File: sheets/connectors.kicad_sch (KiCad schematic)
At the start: 11 parts

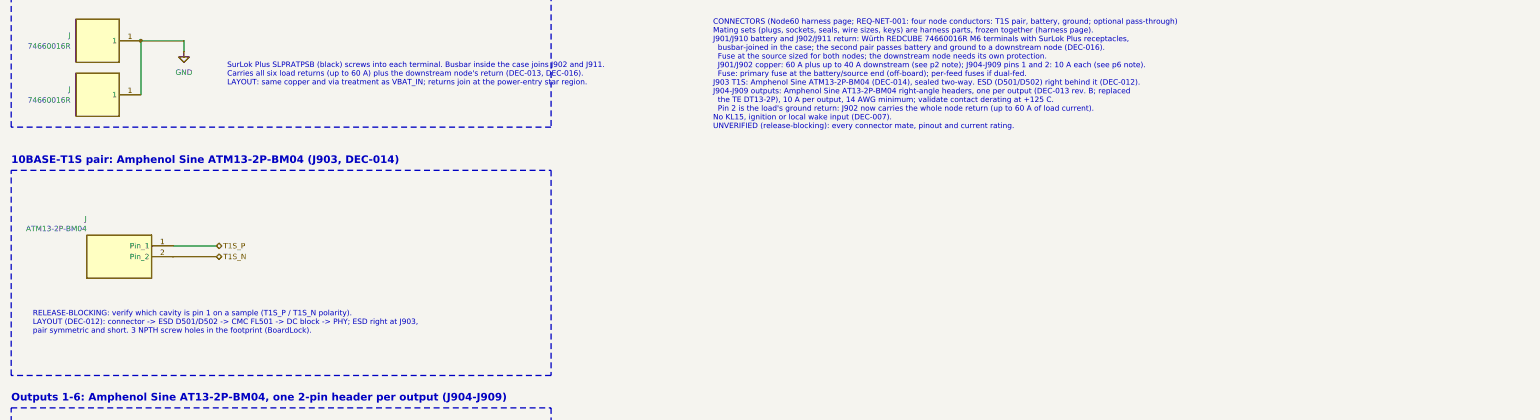
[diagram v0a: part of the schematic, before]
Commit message: DEC-017: T1S bus pass-through and relay-switched termination
The user asked for a second T1S connector so a downstream node can join
the bus, and a termination that can be switched between bus end and
mid-bus (2026-10-28).

- p9: J912, a second ATM13-2P-BM04 in parallel with J903
- p5: R502 (single 100R, not fitted) replaced by the OPEN Alliance
  split termination: latching relay K501 (Omron G6KU-2F-Y-T1-TRS DC3,
  +125 °C) selects 49.9R (end, SET) or 1.5k (drop, RESET) legs to a
  centre tap with 100nF || 100k; Q501/Q502 (DMC2710UVQ-7) half-bridges
  drive the coil from 3V3_MAIN
- p4/root: PTD0 -> T1S_TERM_END, PTD1 -> T1S_TERM_DROP
- Library pinned to dropout-kicad-library PR #37 head db07592; the new
  DropOut_Relay / DropOut_Relay_SMD libraries are in the library tables
- DEC-017, parts, GATE-NET-02 (switched termination), GATE-NET-01 wake
  test in both states, firmware and network pages, GATE-MCU-01 addendum

Co-Authored-By: Claude Opus 5.5 <noreply@anthropic.com>
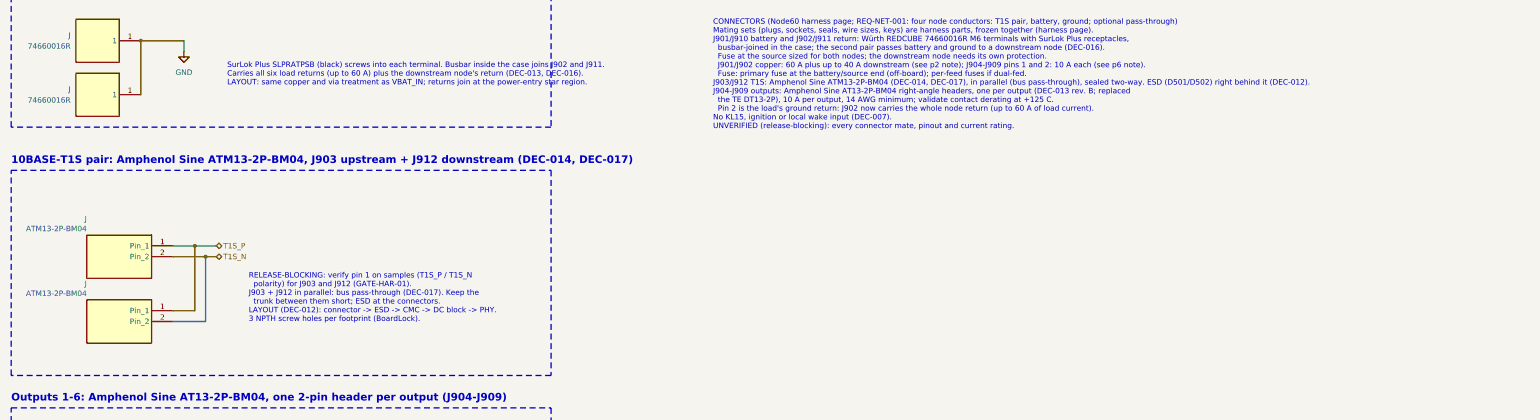
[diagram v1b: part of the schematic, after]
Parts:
- added J: ATM13-2P-BM04, DropOut_Connector_Amphenol:Amphenol_ATM13-2P-BMxx_1x02_P4.20mm_Horizontal, symbol DropOut_Connector:ATM13-2P-BM04
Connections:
- net T1S_N: now also J.2 (Pin_2)
- net T1S_P: now also J.1 (Pin_1)
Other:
- note added: "10BASE-T1S pair: Amphenol Sine ATM13-2P-BM04, J903 upstream + J912 downstream (DEC-014, DEC-017)"
- note added: "RELEASE-BLOCKING: verify pin 1 on samples (T1S_P / T1S_N polarity) for J903 and J912 (GATE-HAR-01). J903 + J912 in parallel: bus pass-through (DEC-017). Keep the trunk between them short; ESD at the connectors. LAYOUT (DEC-012): connector -> ESD -> CMC -> DC block -> PHY. 3 NPTH screw holes per footprint (BoardLock)."
- note removed: "10BASE-T1S pair: Amphenol Sine ATM13-2P-BM04 (J903, DEC-014)"
- note removed: "RELEASE-BLOCKING: verify which cavity is pin 1 on a sample (T1S_P / T1S_N polarity). LAYOUT (DEC-012): connector -> ESD D501/D502 -> CMC FL501 -> DC block -> PHY; ESD right at J903, pair symmetric and short. 3 NPTH screw holes in the footprint (BoardLock)."
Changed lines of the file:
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@@
 		)
 	)
-	(text "10BASE-T1S pair: Amphenol Sine ATM13-2P-BM04 (J903, DEC-014)"
+	(text "10BASE-T1S pair: Amphenol Sine ATM13-2P-BM04, J903 upstream + J912 downstream (DEC-014, DEC-017)"
 		(exclude_from_sim no)
 		(at 25.4 151.13 0)
@@
 		)
 	)
-	(text "RELEASE-BLOCKING: verify which cavity is pin 1 on a sample (T1S_P / T1S_N polarity).\nLAYOUT (DEC-012): connector -> ESD D501/D502 -> CMC FL501 -> DC block -> PHY; ESD right at J903,\npair symmetric and short. 3 NPTH screw holes in the footprint (BoardLock)."
-		(exclude_from_sim no)
-		(at 30.48 185.42 0)
+	(text "RELEASE-BLOCKING: verify pin 1 on samples (T1S_P / T1S_N\n  polarity) for J903 and J912 (GATE-HAR-01).\nJ903 + J912 in parallel: bus pass-through (DEC-017). Keep the\n  trunk between them short; ESD at the connectors.\nLAYOUT (DEC-012): connector -> ESD -> CMC -> DC block -> PHY.\n3 NPTH screw holes per footprint (BoardLock)."
+		(exclude_from_sim no)
+		(at 81.28 176.53 0)
 		(effects
 			(font
@@
 		)
 	)
-	(text "CONNECTORS (Node60 harness page; REQ-NET-001: four node conductors: T1S pair, battery, ground; optional pass-through)\nMating sets (plugs, sockets, seals, wire sizes, keys) are harness parts, frozen together (harness page).\nJ901/J910 battery and J902/J911 return: Würth REDCUBE 74660016R M6 terminals with SurLok Plus receptacles,\n  busbar-joined in the case; the second pair passes battery and ground to a downstream node (DEC-016).\n  Fuse at the source sized for both nodes; the downstream node needs its own protection.\n  J901/J902 copper: 60 A plus up to 40 A downstream (see p2 note); J904-J909 pins 1 and 2: 10 A each (see p6 note).\n  Fuse: primary fuse at the battery/source end (off-board); per-feed fuses if dual-fed.\nJ903 T1S: Amphenol Sine ATM13-2P-BM04 (DEC-014), sealed two-way. ESD (D501/D502) right behind it (DEC-012).\nJ904-J909 outputs: Amphenol Sine AT13-2P-BM04 right-angle headers, one per output (DEC-013 rev. B; replaced\n  the TE DT13-2P), 10 A per output, 14 AWG minimum; validate contact derating at +125 C.\n  Pin 2 is the load's ground return: J902 now carries the whole node return (up to 60 A of load current).\nNo KL15, ignition or local wake input (DEC-007).\nUNVERIFIED (release-blocking): every connector mate, pinout and current rating.\n"
+	(text "CONNECTORS (Node60 harness page; REQ-NET-001: four node conductors: T1S pair, battery, ground; optional pass-through)\nMating sets (plugs, sockets, seals, wire sizes, keys) are harness parts, frozen together (harness page).\nJ901/J910 battery and J902/J911 return: Würth REDCUBE 74660016R M6 terminals with SurLok Plus receptacles,\n  busbar-joined in the case; the second pair passes battery and ground to a downstream node (DEC-016).\n  Fuse at the source sized for both nodes; the downstream node needs its own protection.\n  J901/J902 copper: 60 A plus up to 40 A downstream (see p2 note); J904-J909 pins 1 and 2: 10 A each (see p6 note).\n  Fuse: primary fuse at the battery/source end (off-board); per-feed fuses if dual-fed.\nJ903/J912 T1S: Amphenol Sine ATM13-2P-BM04 (DEC-014, DEC-017), in parallel (bus pass-through), sealed two-way. ESD (D501/D502) right behind it (DEC-012).\nJ904-J909 outputs: Amphenol Sine AT13-2P-BM04 right-angle headers, one per output (DEC-013 rev. B; replaced\n  the TE DT13-2P), 10 A per output, 14 AWG minimum; validate contact derating at +125 C.\n  Pin 2 is the load's ground return: J902 now carries the whole node return (up to 60 A of load current).\nNo KL15, ignition or local wake input (DEC-007).\nUNVERIFIED (release-blocking): every connector mate, pinout and current rating.\n"
 		(exclude_from_sim no)
 		(at 190.5 116.84 0)
@@
 		)
 	)
+	(symbol
+		(lib_id "DropOut_Connector:ATM13-2P-BM04")
+		(at 50.8 187.96 0)
+		(mirror y)
+		(unit 1)
+		(body_style 1)
+		(exclude_from_sim no)
+		(in_bom yes)
+		(on_board yes)
+		(in_pos_files yes)
+		(dnp no)
+		(fields_autoplaced no)
+		(property "Reference" "J"
+			(at 43.18 179.07 0)
+			(effects
+				(font
+					(size 1.27 1.27)
+				)
+				(justify left)
+			)
+		)
+		(property "Value" "ATM13-2P-BM04"
+			(at 43.18 181.37 0)
+			(effects
+				(font
+					(size 1.27 1.27)
+				)
+				(justify left)
+			)
+		)
+		(property "Footprint" "DropOut_Connector_Amphenol:Amphenol_ATM13-2P-BMxx_1x02_P4.20mm_Horizontal"
+			(at 50.8 187.96 0)
+			(effects
+				(font
+					(size 1.27 1.27)
+				)
+				(hide yes)
+			)
+		)
+		(property "Datasheet" "https://www.amphenol-sine.com/pdf/datasheet/ATM13-2P-BM04.pdf"
+			(at 50.8 187.96 0)
+			(effects
+				(font
+					(size 1.27 1.27)
+				)
+				(hide yes)
+			)
+		)
+		(property "Description" "Amphenol Sine BoardLock ATM13 2-pin right-angle PCB receptacle with flange seal, 4.20 mm pitch, tin-plated size 20 pins, potting, 7.5 A, 250 V, IP67 mated, -55 to +125 °C; mates ATM06-2S"
+			(at 50.8 187.96 0)
+			(effects
+				(font
+					(size 1.27 1.27)
+				)
+				(hide yes)
+			)
+		)
+		(property "Manufacturer" "Amphenol Sine Systems"
+			(at 50.8 187.96 0)
+			(effects
+				(font
+					(size 1.27 1.27)
+				)
+				(hide yes)
+			)
+		)
+		(property "MPN" "ATM13-2P-BM04"
+			(at 50.8 187.96 0)
+			(effects
+				(font
+					(size 1.27 1.27)
+				)
+				(hide yes)
+			)
+		)
+		(property "DigiKey_PN" "889-3357-ND"
+			(at 50.8 187.96 0)
+			(effects
+				(font
+					(size 1.27 1.27)
+				)
+				(hide yes)
+			)
+		)
+		(property "Mouser_PN" "654-ATM13-2P-BM04"
+			(at 50.8 187.96 0)
+			(effects
+				(font
+					(size 1.27 1.27)
+				)
+				(hide yes)
+			)
+		)
+		(property "Temperature_Grade" "-55 to +125 °C (not AEC qualified)"
+			(at 50.8 187.96 0)
+			(effects
+				(font
+					(size 1.27 1.27)
+				)
+				(hide yes)
+			)
+		)
+		(property "Notes" "Mates the ATM06-2S plug (size 20 sockets). Fixed by 3x #4-20 thread-forming screws from the solder side (0.68-1.13 N-m). Pin numbering from the drawing's mounting-face view; verify on a sample."
+			(at 50.8 187.96 0)
+			(effects
+				(font
+					(size 1.27 1.27)
+				)
+				(hide yes)
+			)
+		)
+		(pin "1"
+		)
+		(pin "2"
+		)
+		(instances
+			(project "node60"
+				(path "/55f51841-30a3-4965-b848-b796f60054d0/e572f86f-2725-4aae-a9c5-04dc01b6640e"
+					(reference "J912")
+					(unit 1)
+				)
+			)
+		)
+	)
+	(wire
+		(pts
+			(xy 63.5 185.42)
+			(xy 68.58 185.42)
+		)
+		(stroke
+			(width 0)
+			(type default)
+		)
+	)
+	(wire
+		(pts
+			(xy 68.58 185.42)
+			(xy 68.58 170.18)
+		)
+		(stroke
+			(width 0)
+			(type default)
+		)
+	)
+	(wire
+		(pts
+			(xy 63.5 187.96)
+			(xy 71.12 187.96)
+		)
+		(stroke
+			(width 0)
+			(type default)
+		)
+	)
+	(wire
+		(pts
+			(xy 71.12 187.96)
+			(xy 71.12 172.72)
+		)
+		(stroke
+			(width 0)
+			(type default)
+		)
+	)
+	(junction
+		(at 68.58 170.18)
+		(diameter 0)
+		(color 0 0 0 0)
+	)
+	(junction
+		(at 71.12 172.72)
+		(diameter 0)
+		(color 0 0 0 0)
+	)
 	(embedded_fonts no)

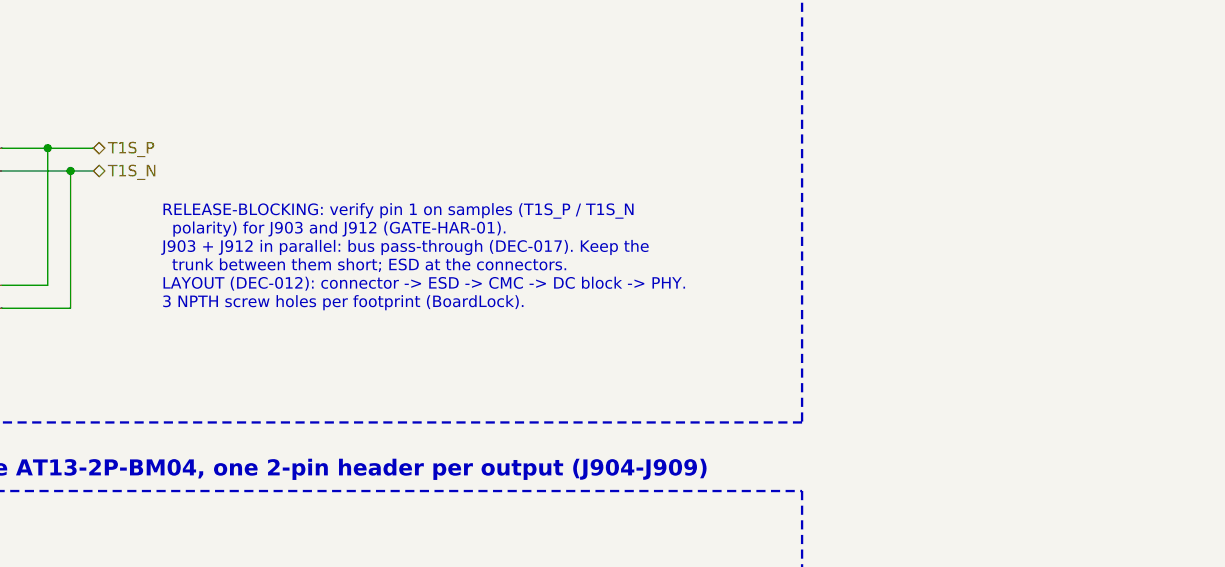
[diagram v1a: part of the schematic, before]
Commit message: DEC-012 rev. B: DC block on the connector side of the choke
Microchip AN1718 rev. D (the LAN8670 data sheet's line-interface
reference), OPEN Alliance's implementation spec (Figure 4) and both
Microchip LAN8670 evaluation boards order the line interface
connector -> ESD -> termination -> DC block -> CMC -> PHY. Node60 had
the choke on the connector side. The user approved the swap on
2026-10-29.

- p5: FL501 moved next to the PHY, C511/C512 to the bus side; no part
  changes; windings unchanged (1-4 P, 2-3 N)
- DEC-012 rev. B with the old order as a rejected option; layout notes
  on p5, p9 and in DEC-017 follow
- AN1718 and the two evaluation board schematics archived in
  dropout-vendor-docs (d4bfad3)

Co-Authored-By: Claude Opus 5.5 <noreply@anthropic.com>
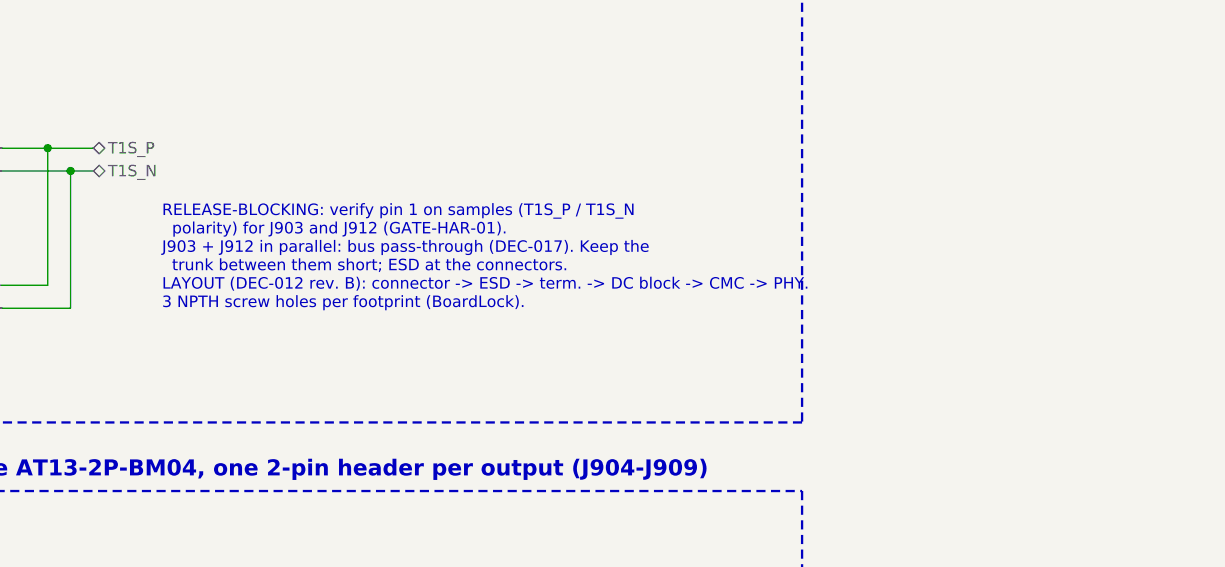
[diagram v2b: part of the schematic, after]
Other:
- note added: "RELEASE-BLOCKING: verify pin 1 on samples (T1S_P / T1S_N polarity) for J903 and J912 (GATE-HAR-01). J903 + J912 in parallel: bus pass-through (DEC-017). Keep the trunk between them short; ESD at the connectors. LAYOUT (DEC-012 rev. B): connector -> ESD -> term. -> DC block -> CMC -> PHY. 3 NPTH screw holes per footprint (BoardLock)."
- note removed: "RELEASE-BLOCKING: verify pin 1 on samples (T1S_P / T1S_N polarity) for J903 and J912 (GATE-HAR-01). J903 + J912 in parallel: bus pass-through (DEC-017). Keep the trunk between them short; ESD at the connectors. LAYOUT (DEC-012): connector -> ESD -> CMC -> DC block -> PHY. 3 NPTH screw holes per footprint (BoardLock)."
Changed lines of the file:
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@@
 		)
 	)
-	(text "RELEASE-BLOCKING: verify pin 1 on samples (T1S_P / T1S_N\n  polarity) for J903 and J912 (GATE-HAR-01).\nJ903 + J912 in parallel: bus pass-through (DEC-017). Keep the\n  trunk between them short; ESD at the connectors.\nLAYOUT (DEC-012): connector -> ESD -> CMC -> DC block -> PHY.\n3 NPTH screw holes per footprint (BoardLock)."
+	(text "RELEASE-BLOCKING: verify pin 1 on samples (T1S_P / T1S_N\n  polarity) for J903 and J912 (GATE-HAR-01).\nJ903 + J912 in parallel: bus pass-through (DEC-017). Keep the\n  trunk between them short; ESD at the connectors.\nLAYOUT (DEC-012 rev. B): connector -> ESD -> term. -> DC block -> CMC -> PHY.\n3 NPTH screw holes per footprint (BoardLock)."
 		(exclude_from_sim no)
 		(at 81.28 176.53 0)

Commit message: DEC-022: enclosure version 4, press-fit terminals and a flat lid
The user chose enclosure version 4 (2026-10-31): a flat lid simplifies
the mechanical design and seals on one level instead of across the
vertical faces of a step.

- DEC-022 (accepted, Rev B, supersedes DEC-021): Würth REDCUBE
  PRESS-FIT 786202106 terminals (180 A, M6 blind thread) on F.Cu with
  the 1/8" x 1" busbars on the blocks; flat 4 mm machined lid with a
  2.6 mm seat and M4 bosses per SurLok receptacle; board 5 mm off the
  floor; removable north panel. DEC-016's receptacles and pass-through
  stand; its terminal part is replaced.
- Parts: 786202106 selected (4), 74660016R now an alternative (0).
- Schematic: J901, J902, J910, J911 -> 786202106 (same one-pin symbol
  and nets).
- PCB: CURRENT = v4; the four terminals placed as press-fit parts on
  F.Cu. DRC with schematic parity clean; schematic conventions OK.
- Docs: harness page, Rev B list, Enclosure options, GATE-HAR-02,
  CLAUDE.md.

Co-Authored-By: Claude Opus 5.5 <noreply@anthropic.com>
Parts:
- J: value 74660016R -> 786202106; footprint DropOut_TerminalBlock_Wuerth:Wuerth_REDCUBE-SMT_WP-SMRT_74660016 -> DropOut_TerminalBlock_Wuerth:Wuerth_REDCUBE-PRESS-FIT_WP-PFIFUA_786202106_PressFit; symbol DropOut_Connector:74660016R -> DropOut_Connector:786202106; MPN 74660016R -> 786202106; Mouser_PN 710-74660016R -> -; Notes Reflow; Ø9.3 non-plated hole in the board for the spigot. 3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 -> Press-fit: insert in one movement, no rework or soldering a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
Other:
- note added: "Battery input and pass-through: Würth 786202106 press-fit (J901, J910, DEC-016, DEC-022)"
- note added: "CONNECTORS (Node60 harness page; REQ-NET-001: four node conductors: T1S pair, battery, ground; optional pass-through) Mating sets (plugs, sockets, seals, wire sizes, keys) are harness parts, frozen together (harness page). J901/J910 battery and J902/J911 return: Würth REDCUBE PRESS-FIT 786202106 M6 terminals with SurLok Plus receptacles, busbar-joined on the terminal blocks (DEC-022); the second 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"
- note added: "Power return and pass-through: Würth 786202106 press-fit (J902, J911, DEC-016, DEC-022)"
- note removed: "Battery input and pass-through: Würth 74660016R (J901, J910, DEC-016)"
- note removed: "CONNECTORS (Node60 harness page; REQ-NET-001: four node conductors: T1S pair, battery, ground; optional pass-through) Mating sets (plugs, sockets, seals, wire sizes, keys) are harness parts, frozen together (harness page). J901/J910 battery and J902/J911 return: Würth REDCUBE 74660016R M6 terminals with SurLok Plus receptacles, busbar-joined in the case; the second pair passes battery and ground 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"
- note removed: "Power return and pass-through: Würth 74660016R (J902, J911, DEC-016)"
